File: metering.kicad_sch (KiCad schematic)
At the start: 42 parts, among them J1 USB_C_Receptacle_USB2.0_16P, J2 Prog, SW1 Reset, SW2 Boot, U1 USBLC6-2SC6, U2 AMS1117-3.3, U3 ESP32-C3-WROOM-02U, U4 74HC14, X1 Screw_Terminal_01x06, X2 Screw_Terminal_01x06, Y1 32.768kHz

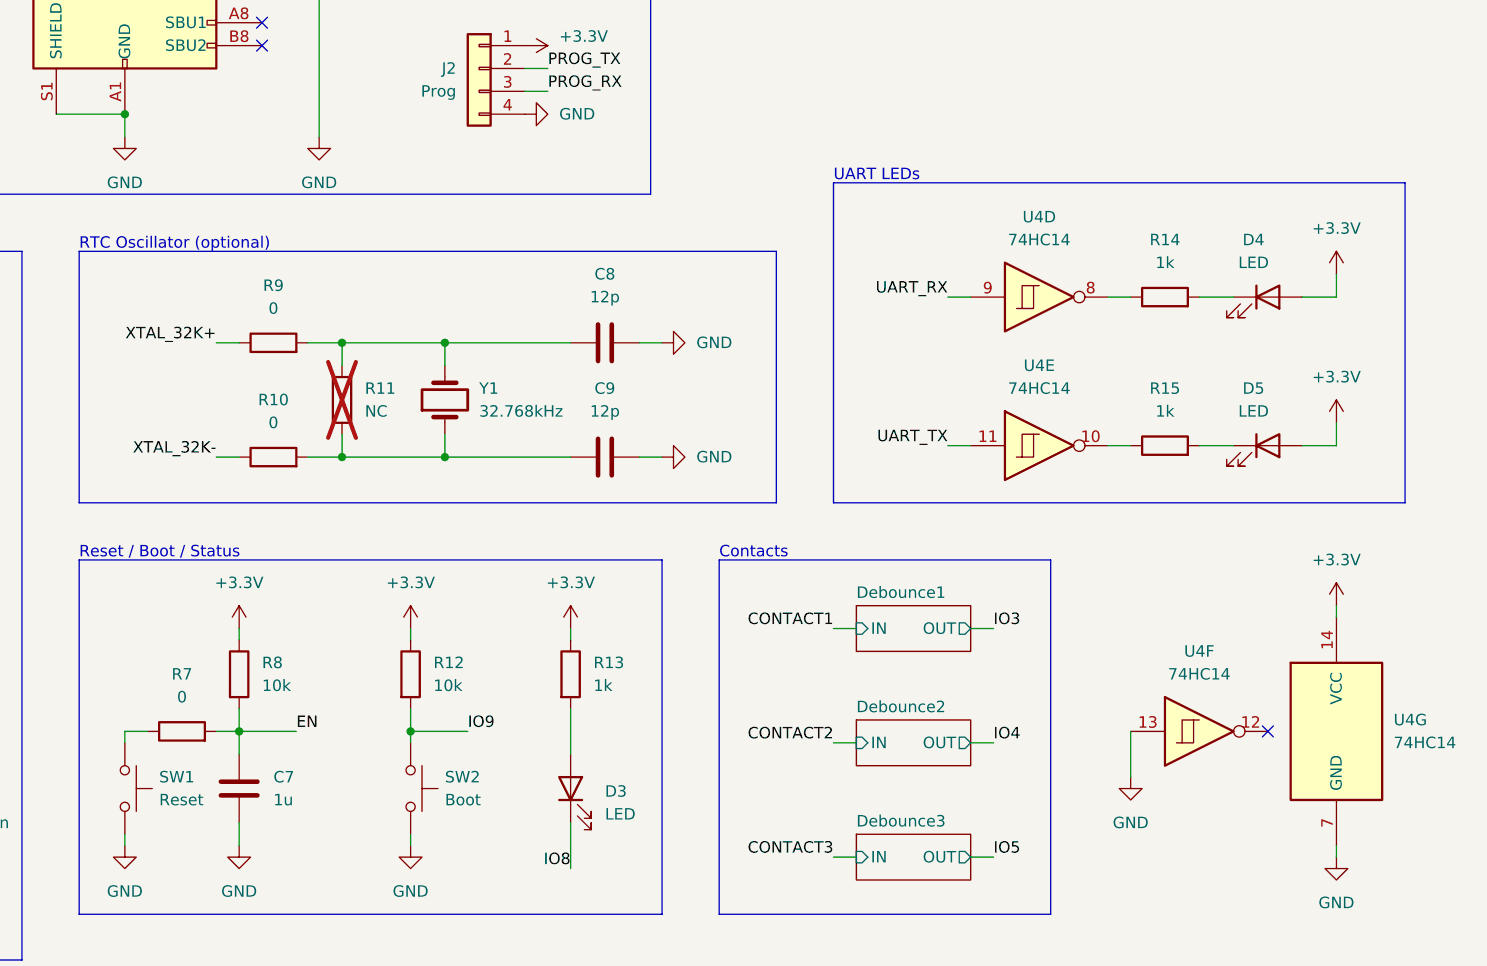
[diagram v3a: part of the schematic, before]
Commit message: Remove UART Tx LED
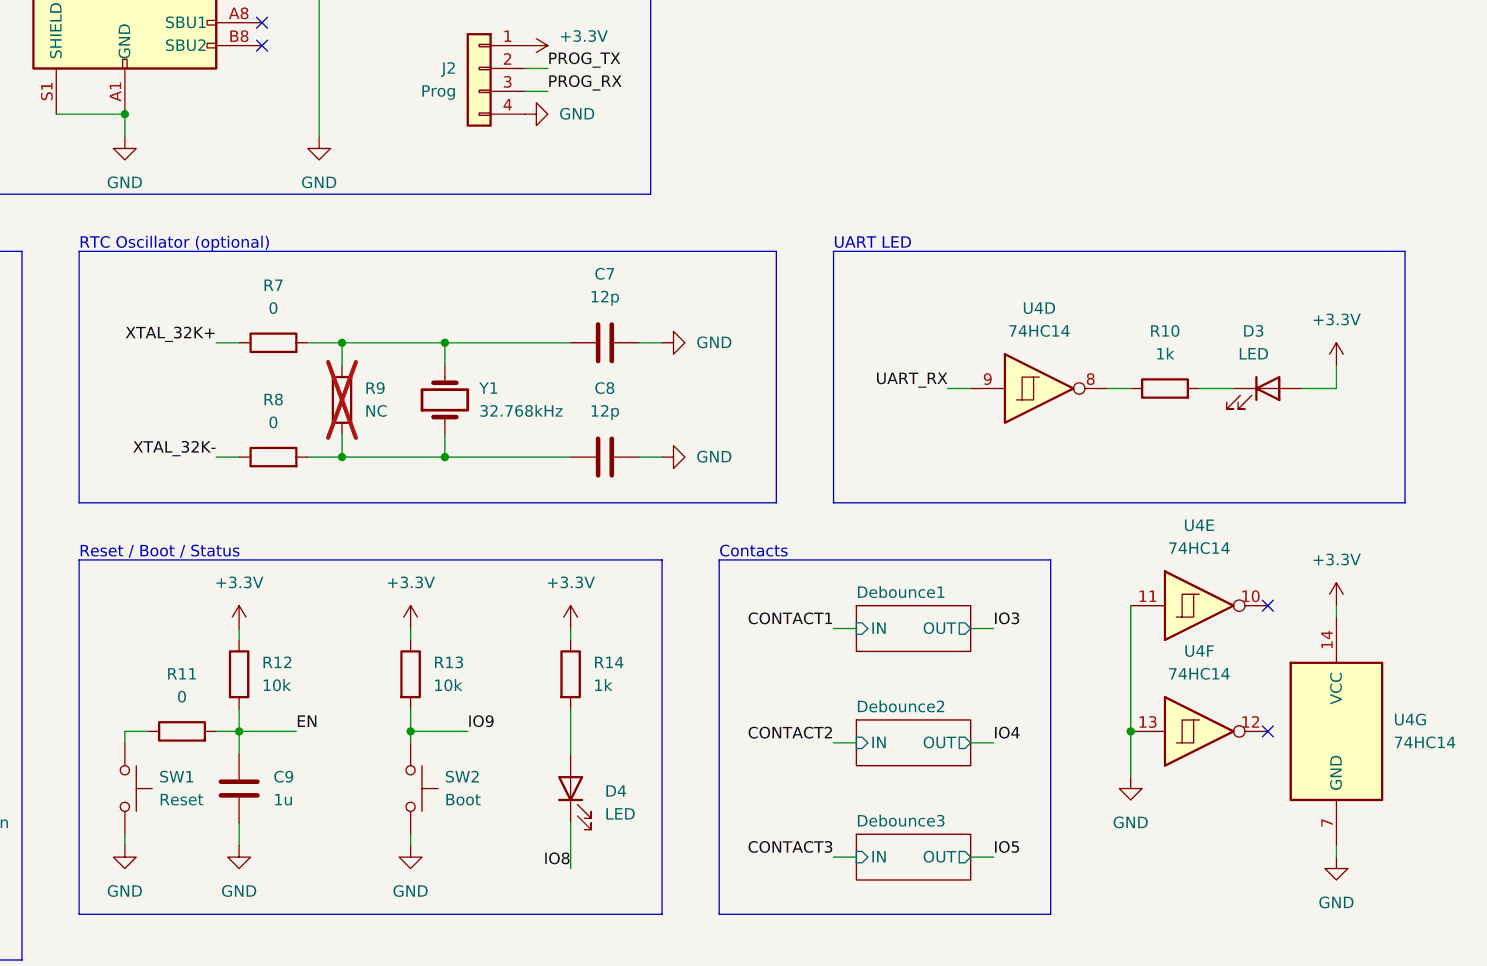
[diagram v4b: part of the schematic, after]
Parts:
- removed D5: LED, LED_THT:LED_D3.0mm_Horizontal_O3.81mm_Z2.0mm, symbol Device:LED
- removed R15: 1k, Resistor_SMD:R_0805_2012Metric, symbol Device:R
- D3: renamed from D4; footprint LED_THT:LED_D3.0mm_Horizontal_O3.81mm_Z2.0mm -> LED_THT:LED_D3.0mm
- D4: renamed from D3; footprint LED_THT:LED_D3.0mm_Horizontal_O3.81mm_Z2.0mm -> LED_THT:LED_D3.0mm
- renumbered C8 to C7, C9 to C8, C7 to C9, R14 to R10, R7 to R11, R8 to R12, R12 to R13, R13 to R14, R9 to R7, R10 to R8, R11 to R9
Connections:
- net GND: now also U4.11
- net UART_TX: no longer U4.11
- no-connect marks 4 -> 5
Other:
- note added: "UART LED"
- note removed: "UART LEDs"
- moved on the sheet: D3, R10, U4D, U4E

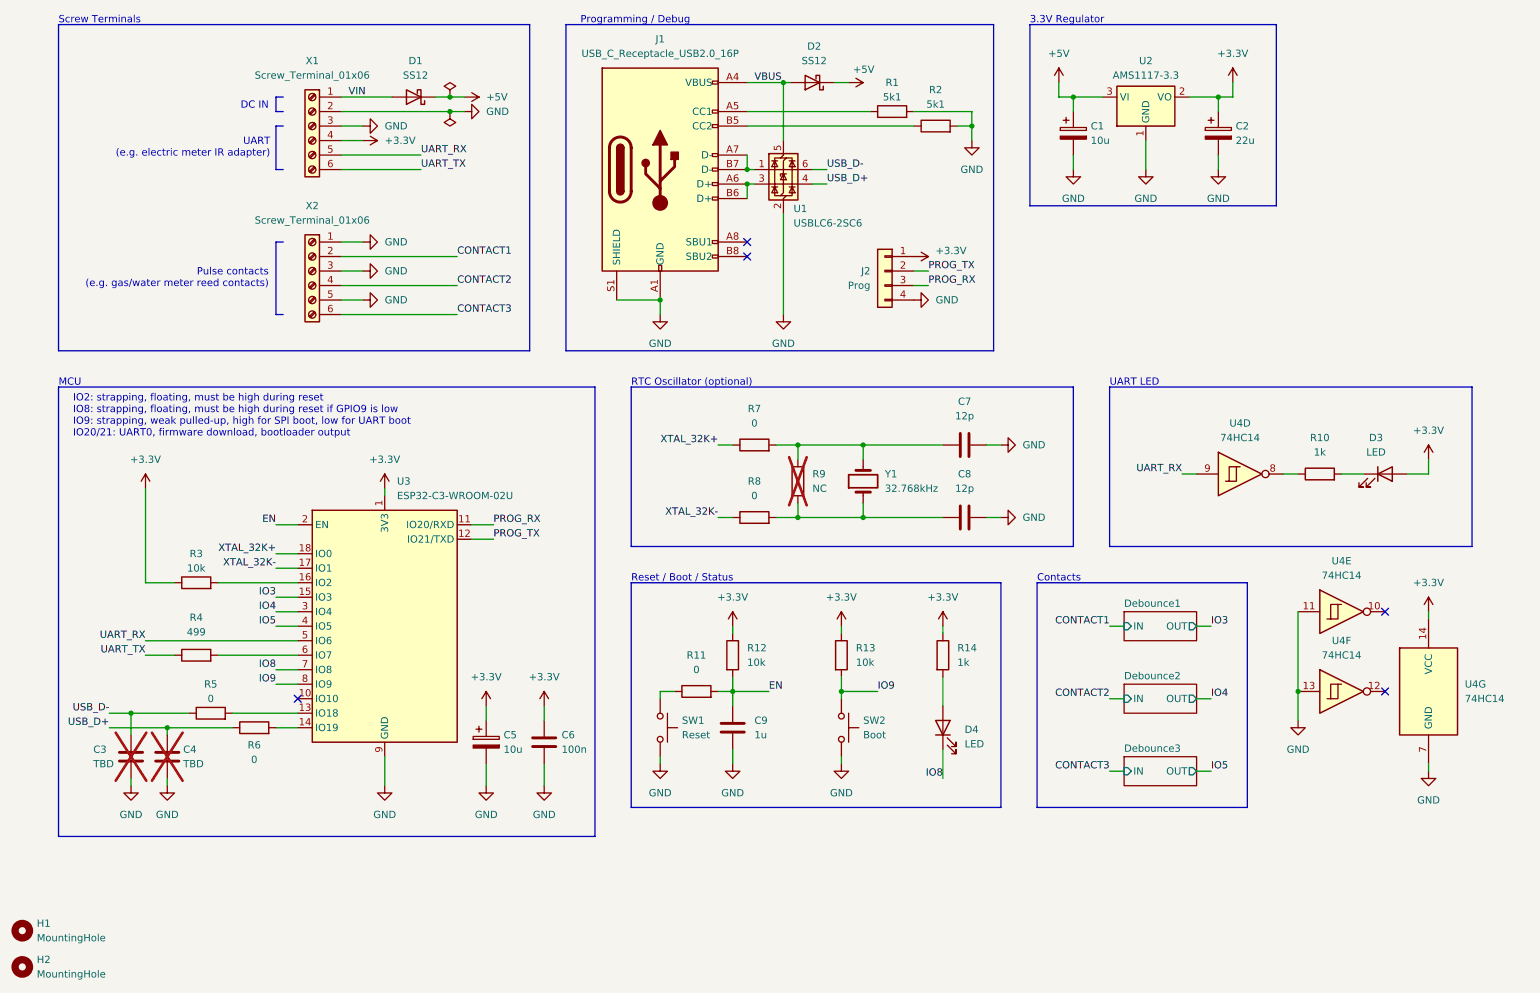
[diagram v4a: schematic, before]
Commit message: Refactor screw terminals and power supply
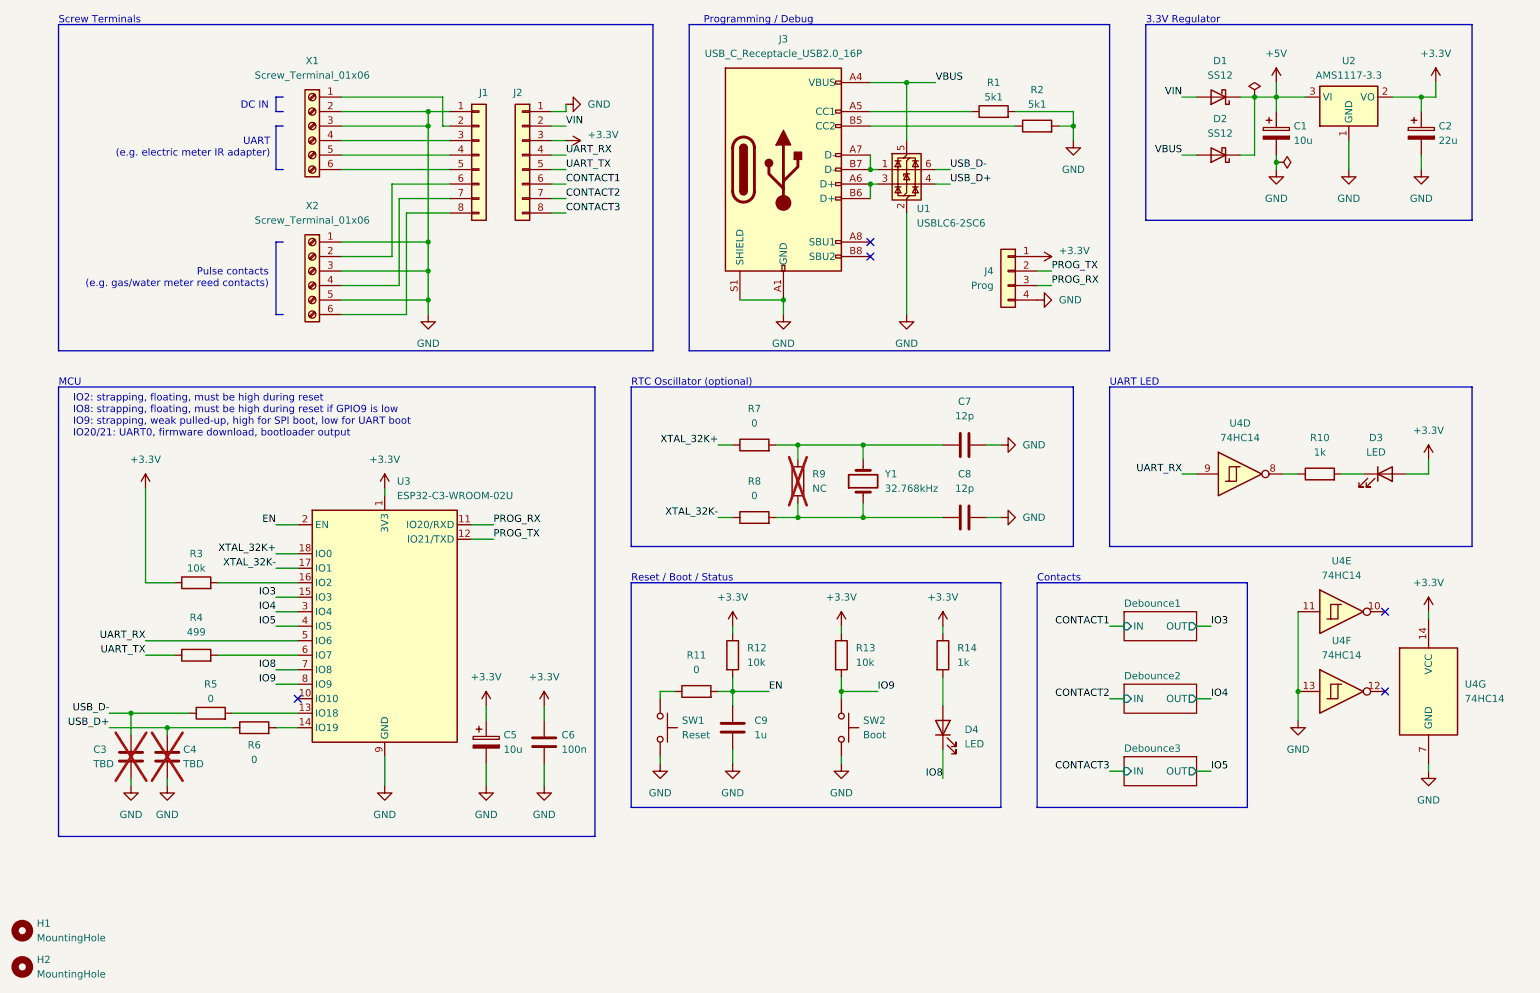
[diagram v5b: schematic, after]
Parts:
- added J1: Conn_01x08, Connector_PinSocket_2.54mm:PinSocket_1x08_P2.54mm_Vertical, symbol Connector_Generic:Conn_01x08
- added J2: Conn_01x08, Connector_PinHeader_2.54mm:PinHeader_1x08_P2.54mm_Horizontal, symbol Connector_Generic:Conn_01x08
- renumbered J1 to J3, J2 to J4
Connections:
- net +3.3V: now also J2.3 (Pin_3); no longer X1.4 (Pin_4)
- net CONTACT1: now also J2.6 (Pin_6); no longer X2.2 (Pin_2)
- net CONTACT2: now also J2.7 (Pin_7); no longer X2.4 (Pin_4)
- net CONTACT3: now also J2.8 (Pin_8); no longer X2.6 (Pin_6)
- net GND: now also J1.1 (Pin_1), J2.1 (Pin_1)
- net UART_RX: now also J2.4 (Pin_4); no longer X1.5 (Pin_5)
- net UART_TX: now also J2.5 (Pin_5); no longer X1.6 (Pin_6)
- net VIN: now also J2.2 (Pin_2); no longer X1.1 (Pin_1)
- new net: J1.6 (Pin_6), X2.2 (Pin_2)
- new net: J1.7 (Pin_7), X2.4 (Pin_4)
- new net: J1.8 (Pin_8), X2.6 (Pin_6)
- new net: J1.2 (Pin_2), X1.1 (Pin_1)
- new net: J1.3 (Pin_3), X1.4 (Pin_4)
- new net: J1.4 (Pin_4), X1.5 (Pin_5)
- new net: J1.5 (Pin_5), X1.6 (Pin_6)
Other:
- moved on the sheet: C1, C2, D1, D2, J3, J4, R1, R2, U1, U2

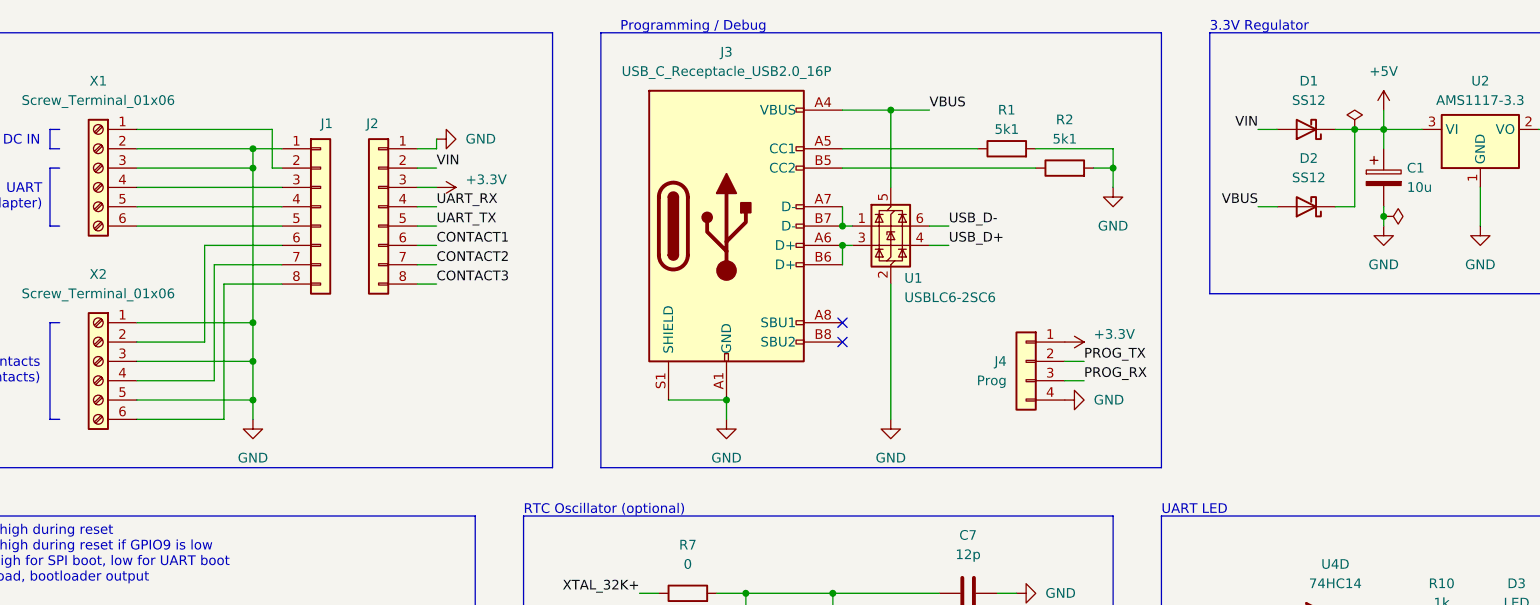
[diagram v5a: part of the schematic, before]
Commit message: Fix base plate separation and power flags
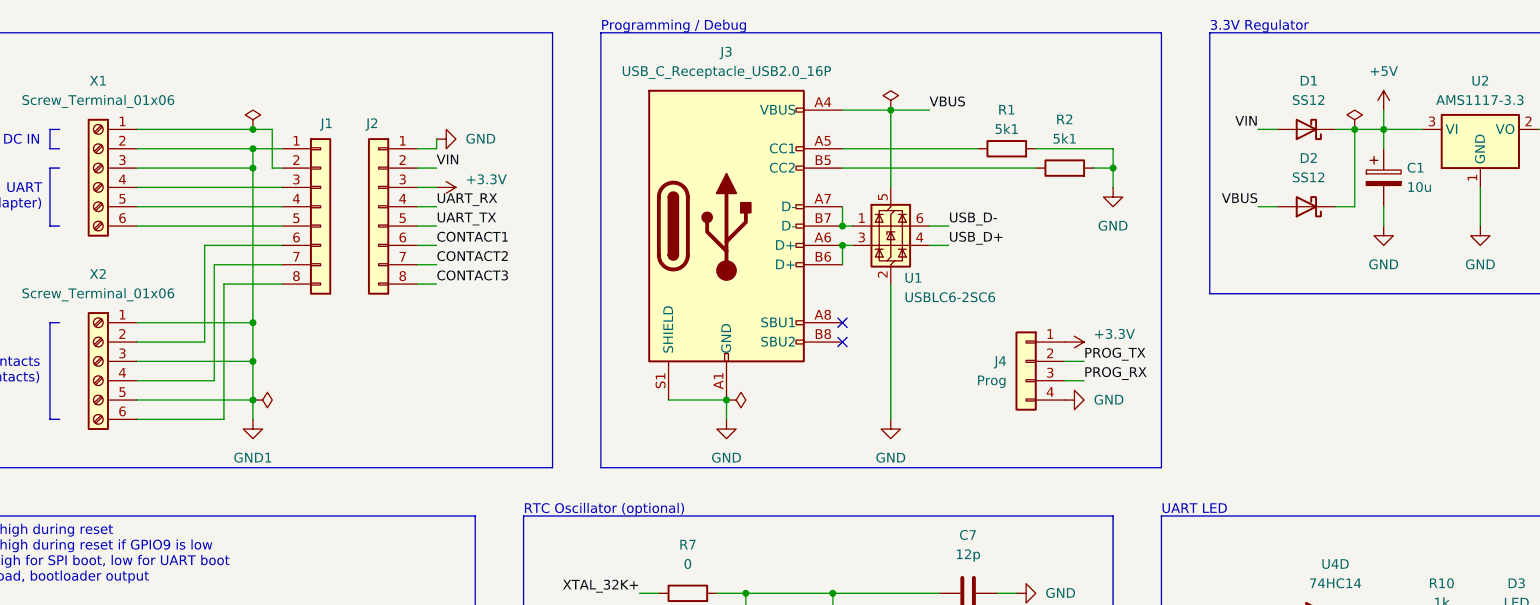
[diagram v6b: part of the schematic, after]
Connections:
- net GND: no longer J1.1 (Pin_1), X1.2 (Pin_2), X1.3 (Pin_3), X2.1 (Pin_1), X2.3 (Pin_3), X2.5 (Pin_5)
- new net GND1: J1.1 (Pin_1), X1.2 (Pin_2), X1.3 (Pin_3), X2.1 (Pin_1), X2.3 (Pin_3), X2.5 (Pin_5)
